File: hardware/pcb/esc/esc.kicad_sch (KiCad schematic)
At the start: 20 parts, among them IC1 DRV8300DPWR, J1 ESC_INPUTS, J2 PHASE_A, J3 PHASE_B, J4 PHASE_C, J7 STM32_STLINK, U1 STM32G071KBT6

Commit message: feat(esc): finished wiring up the mosfets with the amplifier
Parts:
- added C8: 0.1uF, symbol Device:C
- added C9: 100nF, symbol Device:C
- added Q1, Q2, Q3, Q4, Q5, Q6: BSC014N04LS, Package_TO_SOT_SMD:TDSON-8-1, symbol Transistor_FET:BSC13DN30NSFD
- added R10, R9: 10R, symbol Device:R
- added R8: 0.5mR, symbol Device:R
- added U2: INA181A1IDBVR, DBV0006A_N, symbol INA181A1IDBVR:INA181A1IDBVR
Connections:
- net SHA is gone; now on net PHASE_A: C5.1, IC1.18 (SHA)
- net SHB is gone; now on net PHASE_B: C6.1, IC1.15 (SHB)
- net SHC is gone; now on net PHASE_C: C7.1, IC1.12 (SHC)
- net +3.3V: now also C8.1, U2.6 (V+)
- net +VBAT: now also Q1.5 (D), Q3.5 (D), Q5.5 (D)
- net GHA: now also Q1.4 (G)
- net GHB: now also Q3.4 (G)
- net GHC: now also Q5.4 (G)
- net GLB: now also Q4.4 (G); no longer R7.1
- net GLC: now also Q6.4 (G)
- net GND: now also C8.2, R10.2, R8.1, U2.2 (GND), U2.5 (REF); no longer U1.5 (VSS)
- net PHASE_C: now reaches J4.1 (Pin_1)
- net PHASE_C: now also Q5.1 (S), Q5.2 (S), Q5.3 (S), Q6.5 (D)
- net PHASE_B: now reaches J3.1 (Pin_1)
- net PHASE_B: now also Q3.1 (S), Q3.2 (S), Q3.3 (S), Q4.5 (D)
- net CURR_SENSE: now reaches U1.7 (PA0)
- net CURR_SENSE: now also U2.1 (OUT)
- net PHASE_A: now reaches J2.1 (Pin_1)
- net PHASE_A: now also Q1.1 (S), Q1.2 (S), Q1.3 (S), Q2.5 (D)
- new net: Q2.1 (S), Q2.2 (S), Q2.3 (S), Q4.1 (S), Q4.2 (S), Q4.3 (S), Q6.1 (S), Q6.2 (S), Q6.3 (S), R8.2, R9.2
- new net: C9.2, R10.1, U2.4 (IN-)
- new net: C9.1, R9.1, U2.3 (IN+)
- new net GLA: Q2.4 (G), R7.1
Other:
- moved on the sheet: C1, C2, J2, J3, J4, U1

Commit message: feat(fc): fixed buck reg caps' and resistors' value
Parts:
- added C17: 33pF, symbol Device:C
- added C18: 4.7uF, symbol Device:C
- added C19: 100nF, symbol Device:C
- added C20: 10uF, symbol Device:C
- added C21, C22: 1uF, symbol Device:C
- added D1: D_Zener, symbol Device:D_Zener
- added L1: 6.8uH, symbol Device:L
- added R11: 8.9kR, symbol Device:R
- added R12: 47kR, symbol Device:R
- added U5: MP2451DJ-LF-Z, 1_Others:TSOT23-6_MP2451_MNP, symbol MP2451DJ-LF-Z:MP2451DJ-LF-Z
- added U6: AP2112K-3.3TRG1, 1_Others:AP2112K-3.3TRG1, symbol AP2112K-3.3TRG1:AP2112K-3.3TRG1
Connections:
- net +3.3V: now also C22.1, U6.5 (VOUT)
- net GND: now also C18.2, C20.2, C21.2, C22.2, D1.2 (A), R11.1, U5.2 (GND), U6.2 (GND)
- new net: C19.2, D1.1 (K), L1.1, U5.6 (SW)
- new net: C19.1, U5.1 (BST)
- new net: C17.1, R11.2, R12.2, U5.3 (FB)
- new net +5V: C21.1, U6.1 (VIN), U6.3 (EN)
- new net +5V_BAT: C17.2, C20.1, L1.2, R12.1
- new net VOUT_LIPO: C18.1, U5.4 (EN), U5.5 (VIN)
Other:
- note added: "Buck Reg"
- note added: "Driver"
- note added: "LDO"
- note added: "Mosfets"
- moved on the sheet: C1, C2, C3, C4, C5, C6, C7, C8, C9, IC1, Q1, Q2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

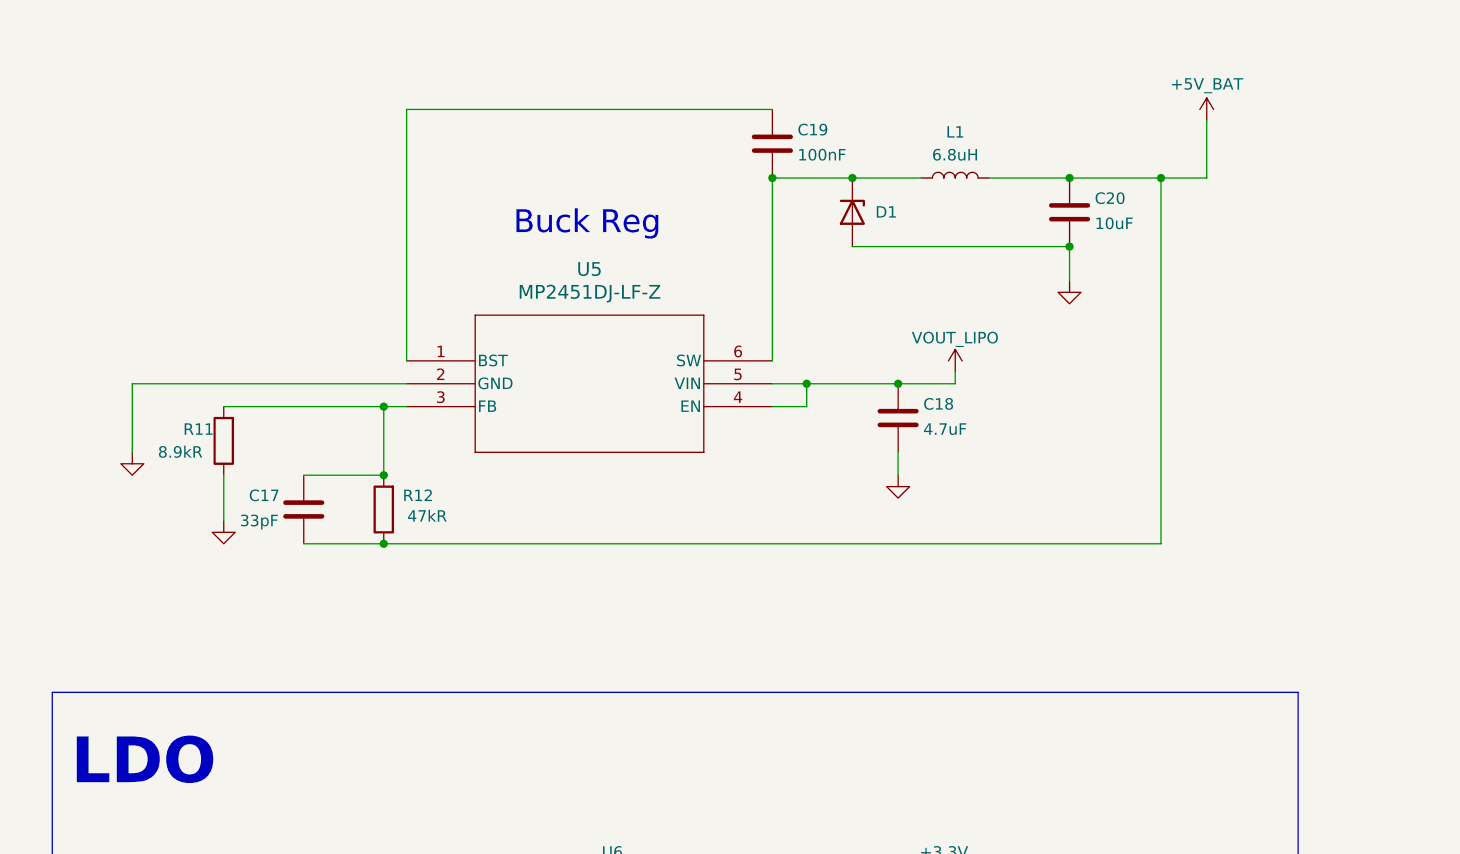
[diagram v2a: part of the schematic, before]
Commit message: feat(esc): config buck reg to 12v
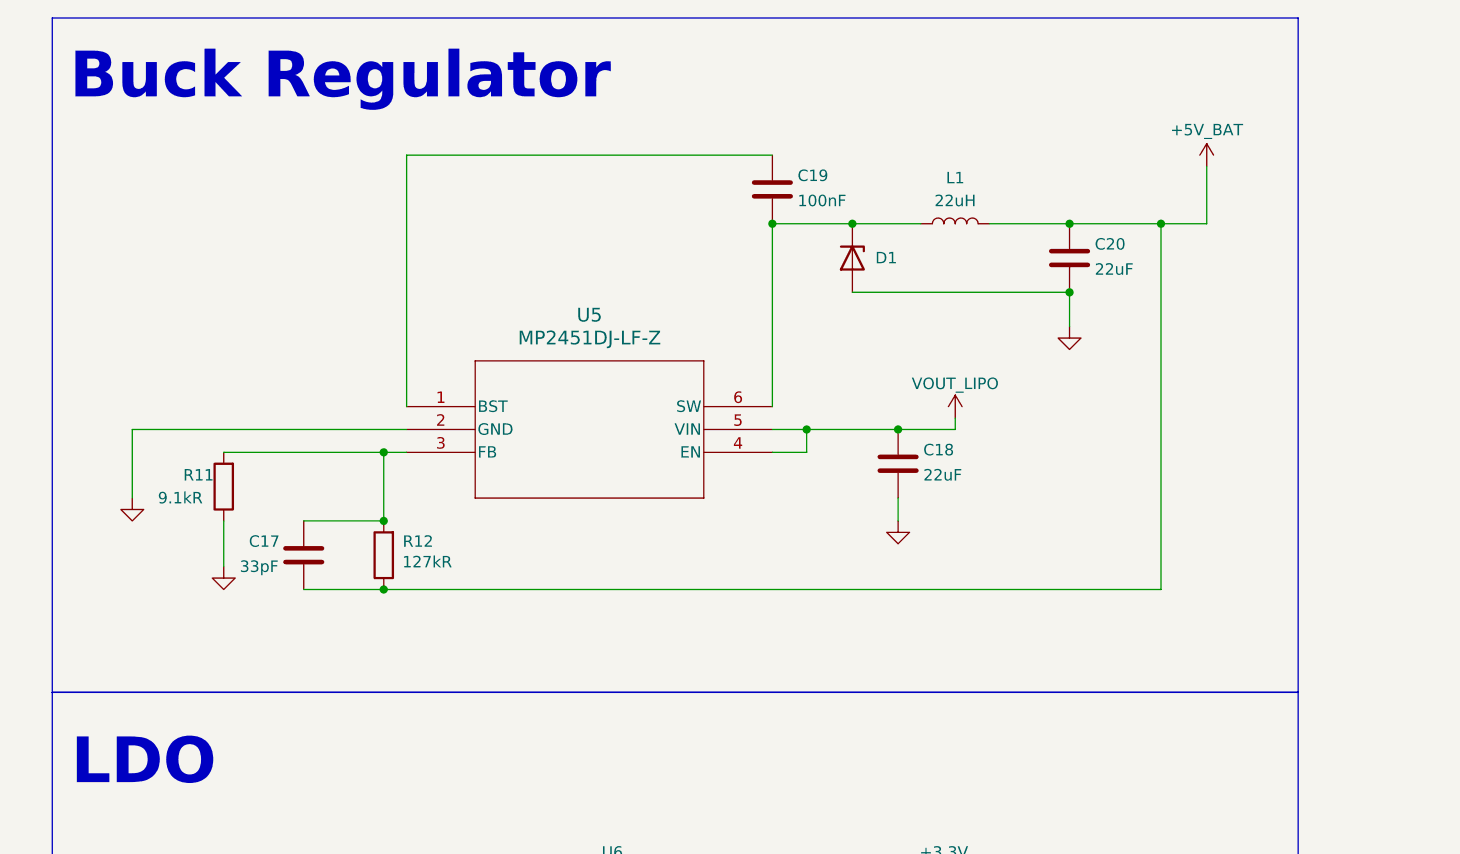
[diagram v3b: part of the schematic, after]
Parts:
- C18: value 4.7uF -> 22uF
- C20: value 10uF -> 22uF
- L1: value 6.8uH -> 22uH
- R11: value 8.9kR -> 9.1kR
- R12: value 47kR -> 127kR
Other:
- note added: "Buck Regulator"
- note removed: "Buck Reg"
- moved on the sheet: C17, C18, C19, C20, D1, L1, R11, R12, U5

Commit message: feat(esc): finished esc schematics
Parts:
- added C10: 100nF, symbol Device:C
- added C23, C24, C25: 10nF, symbol Device:C
- added R12, R13, R14: 75kR, symbol Device:R
- added R18, R19, R20, R21, R22: 10kR, symbol Device:R
- renumbered R11 to R10, R12 to R11, R7 to R4, R6 to R5, R5 to R6, R8 to R7, R9 to R8, R10 to R9
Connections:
- net +3.3V: now also C10.1, R21.2
- net GND: now also U1.5 (VSS), C10.2, C23.2, C24.2, C25.2, R18.1, R19.1, R20.1, R22.1; no longer U2.5 (REF)
- net PHASE_A: now also R12.2
- net PHASE_B: now also R13.2
- net PHASE_C: now also R14.2
- net ADC_C: now reaches U1.10 (PA3)
- net ADC_C: now also C25.1, R14.1, R20.2
- net ADC_A: now reaches U1.8 (PA1)
- net ADC_A: now also C23.1, R12.1, R18.2
- net ADC_B: now reaches U1.9 (PA2)
- net ADC_B: now also C24.1, R13.1, R19.2
- new net +1.65V: R21.1, R22.2, U2.5 (REF)
- no-connect marks 0 -> 16
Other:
- note added: "BEMF"
- note added: "MCU"
- title: (none) -> IamAerial (Drone ESC)
- moved on the sheet: C1, C17, C18, C19, C2, C20, C21, C22, C3, C4, C5, C6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
